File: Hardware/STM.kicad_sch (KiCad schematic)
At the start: 22 parts, among them SW1 Reset, U5 LM4040C33FTA, U6 STM32G484RETx

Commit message: Changes in CAN section
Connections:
- net STBY_CAN_1: now reaches U6.3 (PC14)
- net STBY_CAN_2: now reaches U6.4 (PC15)
- no-connect marks 23 -> 21
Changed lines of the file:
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@@
-	)
-	(no_connect
-		(at 121.92 119.38)
 	)
 	(no_connect
@@
 	(no_connect
 		(at 121.92 83.82)
-	)
-	(no_connect
-		(at 121.92 116.84)
 	)
 	(no_connect
@@
 	(wire
 		(pts
+			(xy 118.11 116.84) (xy 121.92 116.84)
+		)
+		(stroke
+			(width 0)
+			(type default)
+		)
+	)
+	(wire
+		(pts
 			(xy 186.69 27.94) (xy 186.69 30.48)
 		)
@@
 		(pts
 			(xy 186.69 35.56) (xy 186.69 39.37)
+		)
+		(stroke
+			(width 0)
+			(type default)
+		)
+	)
+	(wire
+		(pts
+			(xy 118.11 119.38) (xy 121.92 119.38)
 		)
 		(stroke
@@
 		(effects
 			(font
+				(size 1.27 1.27)
+			)
+			(justify right)
+		)
+	)
+	(hierarchical_label "STBY_CAN_2"
+		(shape output)
+		(at 118.11 119.38 180)
+		(effects
+			(font
+				(size 1.27 1.27)
+			)
+			(justify right)
+		)
+	)
+	(hierarchical_label "STBY_CAN_1"
+		(shape output)
+		(at 118.11 116.84 180)
+		(effects
+			(font

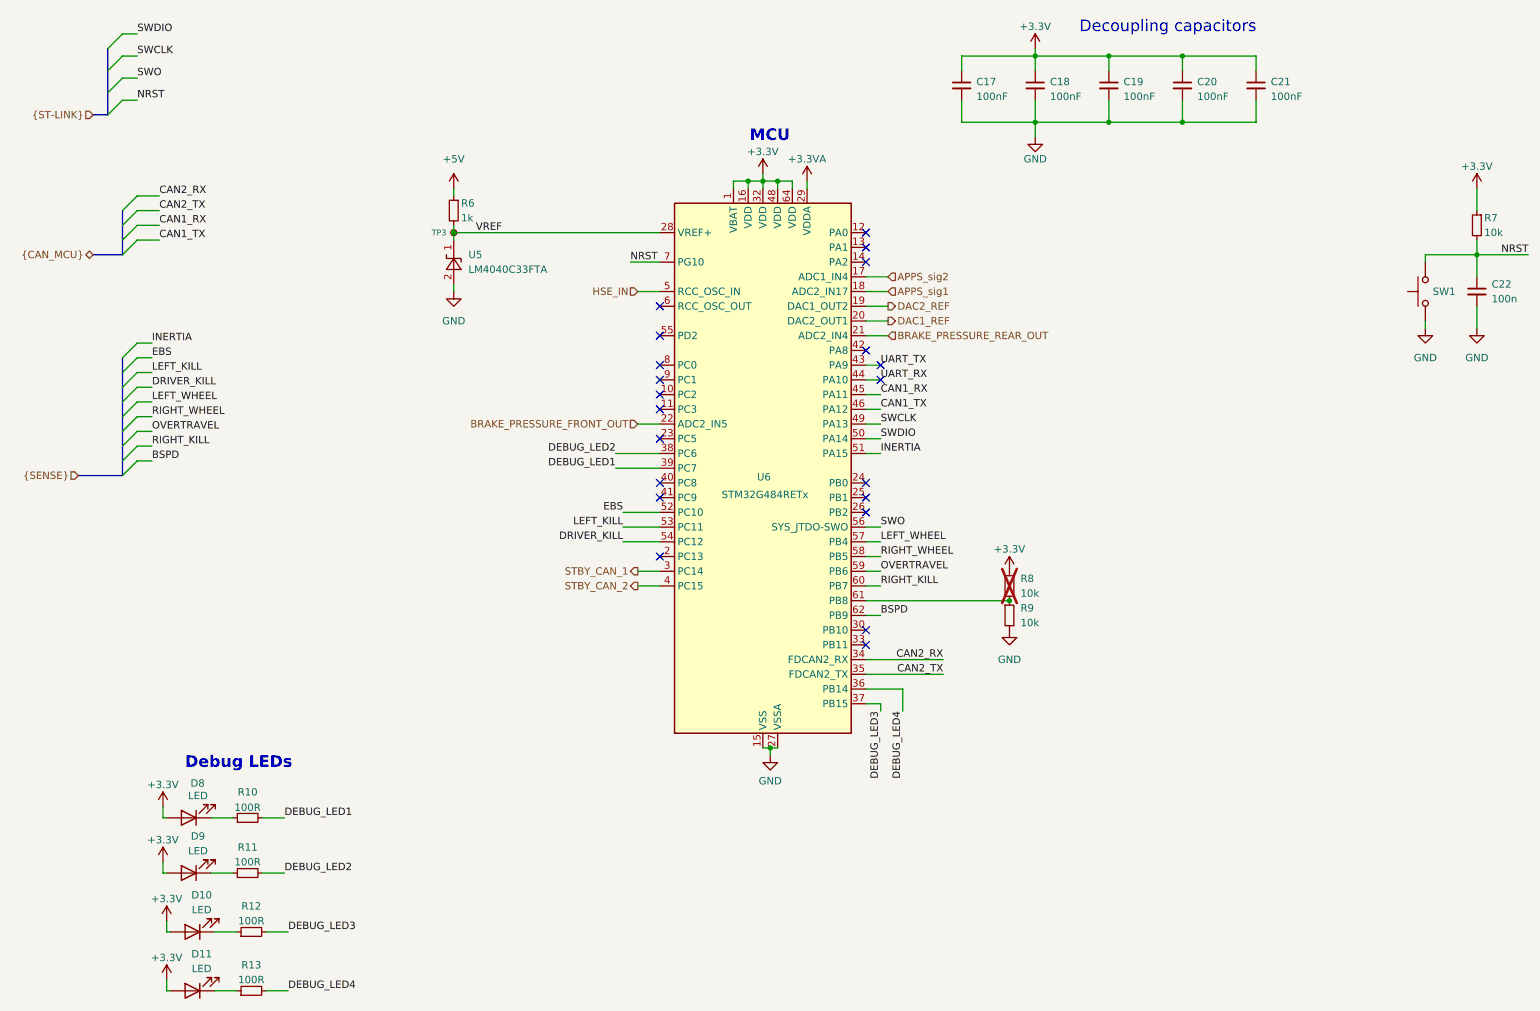
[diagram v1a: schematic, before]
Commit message: Changes in schematic, separated CAN buses, added XIAO Sense S3 DevBoard
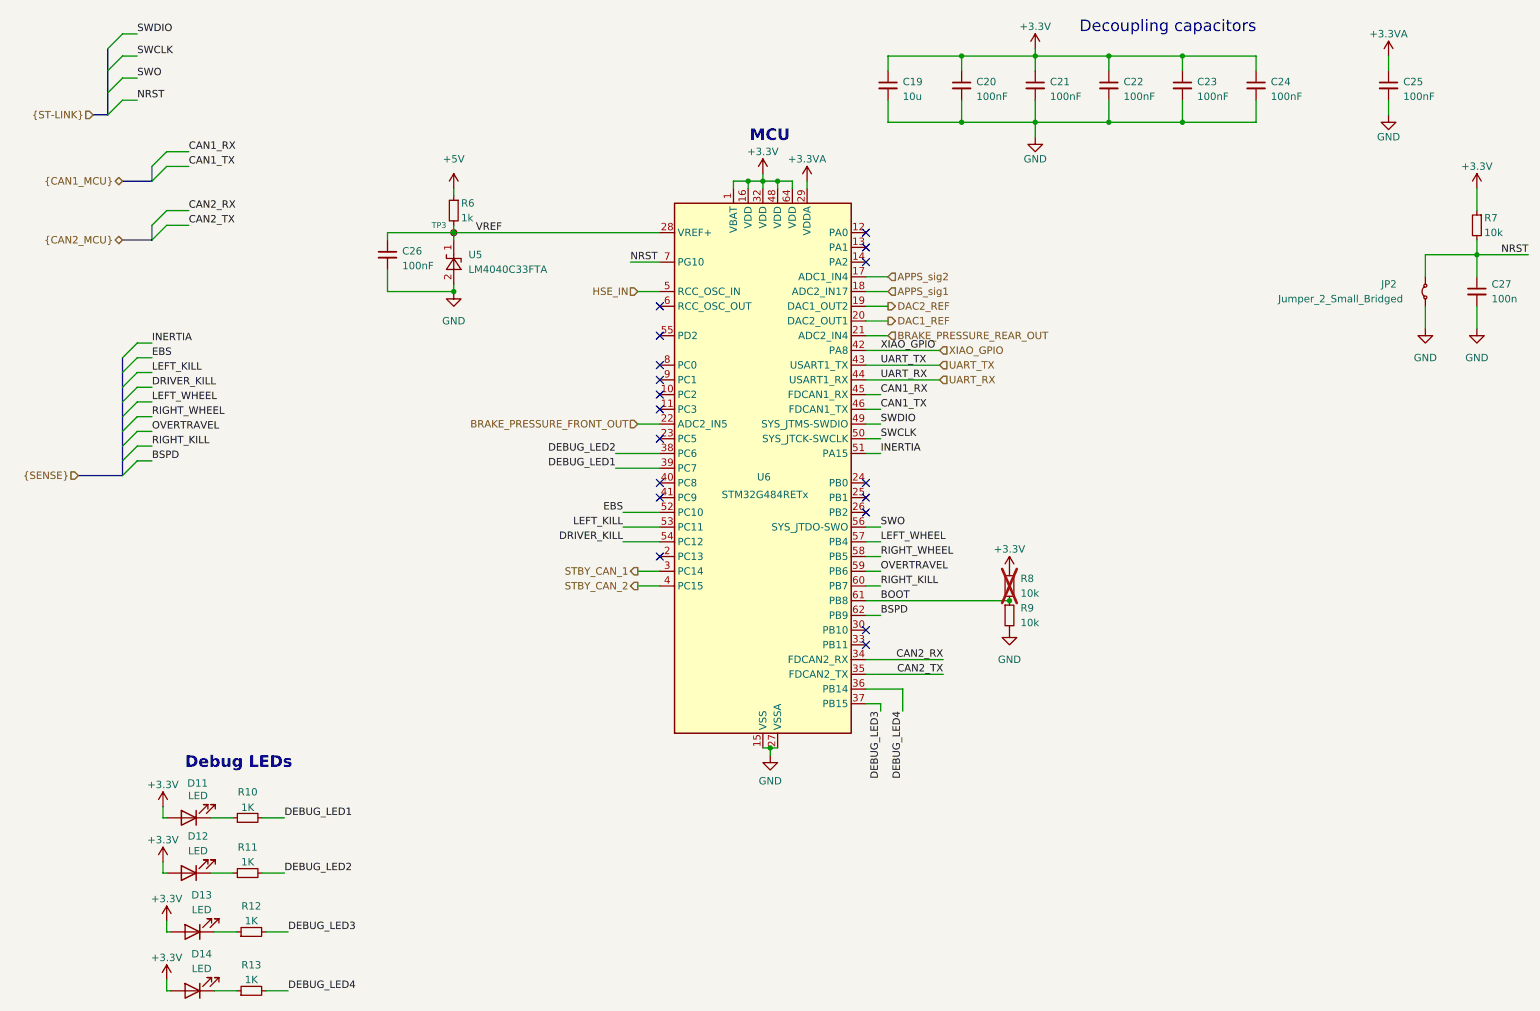
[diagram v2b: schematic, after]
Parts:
- removed SW1: Reset, Button_Switch_SMD:SW_SPST_B3U-1000P, symbol Switch:SW_Push
- added C19: 10u, Capacitor_SMD:C_0805_2012Metric_Pad1.18x1.45mm_HandSolder, symbol Device:C_Small
- added C25, C26: 100nF, Capacitor_SMD:C_0603_1608Metric_Pad1.08x0.95mm_HandSolder, symbol Device:C_Small
- added JP2: Jumper_2_Small_Bridged, Jumper:SolderJumper-2_P1.3mm_Open_TrianglePad1.0x1.5mm, symbol Jumper:Jumper_2_Small_Bridged
- R10, R11, R12, R13: value 100R -> 1K
- renumbered C17 to C20, C18 to C21, C19 to C22, C20 to C23, C21 to C24, C22 to C27, D8 to D11, D9 to D12, D10 to D13, D11 to D14
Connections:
- net +3.3V: now also C19.1
- net +3.3VA: now also C25.1
- net GND: now also C19.2, C25.2, C26.2, JP2.1 (A)
- net NRST: now also JP2.2 (B)
- net SWCLK: now also U6.50 (PA14); no longer U6.49 (PA13)
- net SWDIO: now also U6.49 (PA13); no longer U6.50 (PA14)
- net VREF: now also C26.1
- net BOOT: now reaches R8.2, R9.1, U6.61 (PB8)
- net XIAO_GPIO: now reaches U6.42 (PA8)
- no-connect marks 21 -> 18

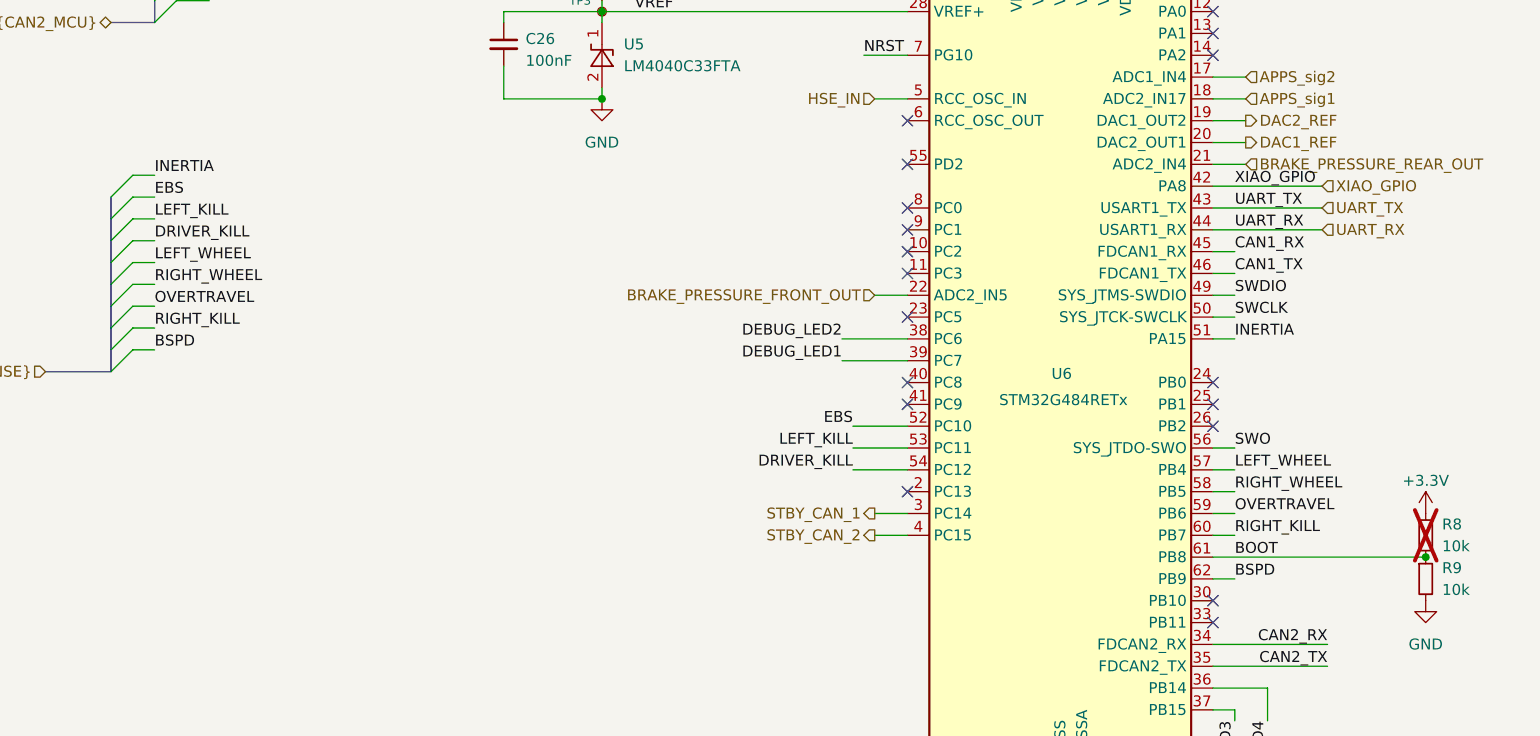
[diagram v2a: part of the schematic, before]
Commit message: Initial layout, changes in safety sensing bus labels
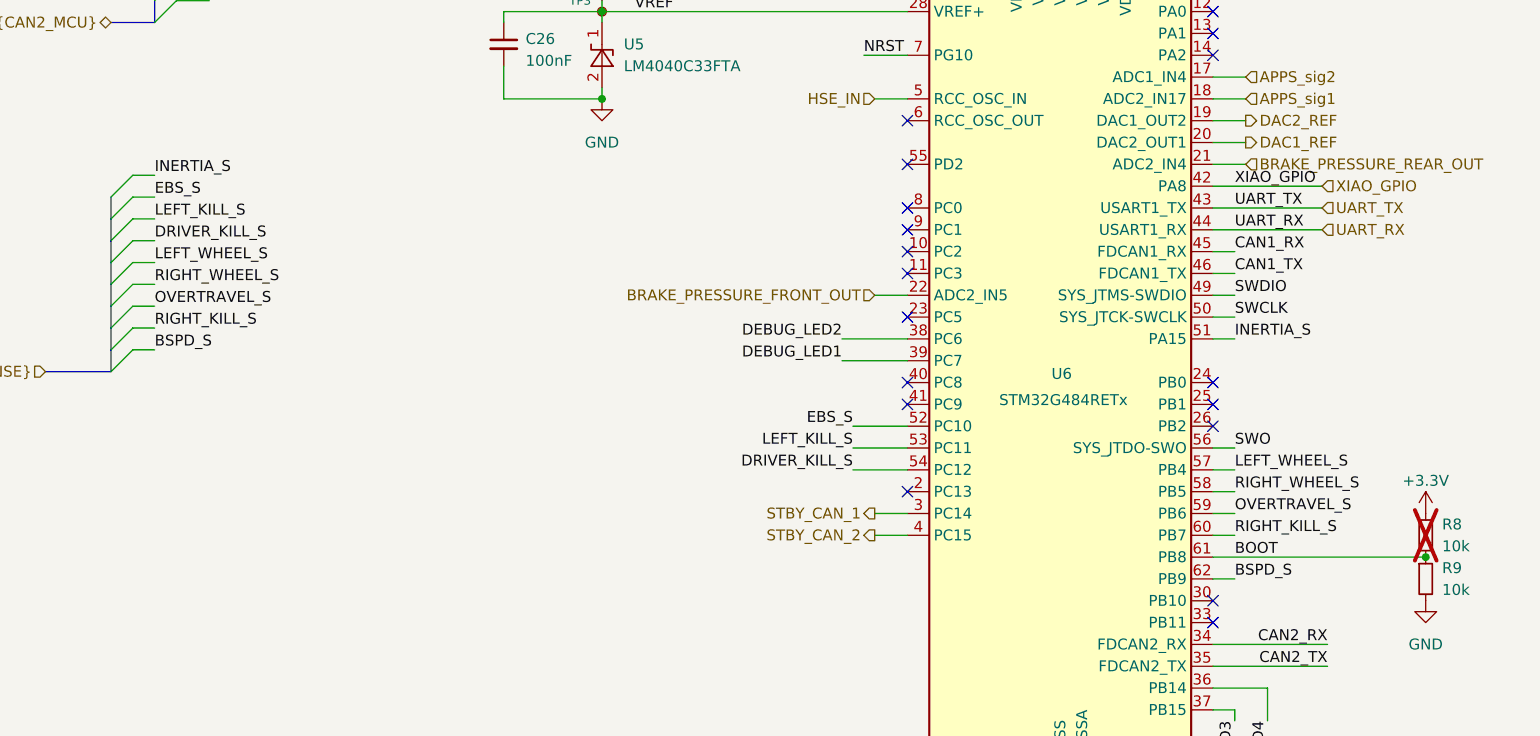
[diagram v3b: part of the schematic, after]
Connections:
- net BSPD renamed BSPD_S
- net DRIVER_KILL renamed DRIVER_KILL_S
- net EBS renamed EBS_S
- net INERTIA renamed INERTIA_S
- net LEFT_KILL renamed LEFT_KILL_S
- net LEFT_WHEEL renamed LEFT_WHEEL_S
- net OVERTRAVEL renamed OVERTRAVEL_S
- net RIGHT_KILL renamed RIGHT_KILL_S
- net RIGHT_WHEEL renamed RIGHT_WHEEL_S
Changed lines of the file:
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@@
 		)
 	)
-	(label "OVERTRAVEL"
+	(label "OVERTRAVEL_S"
 		(at 160.02 116.84 0)
 		(effects
@@
 		)
 	)
-	(label "LEFT_KILL"
+	(label "LEFT_KILL_S"
 		(at 115.57 109.22 180)
 		(effects
@@
 		)
 	)
-	(label "INERTIA"
+	(label "INERTIA_S"
 		(at 34.29 77.47 0)
 		(effects
@@
 		)
 	)
-	(label "BSPD"
+	(label "BSPD_S"
 		(at 34.29 97.79 0)
 		(effects
@@
 		)
 	)
-	(label "DRIVER_KILL"
+	(label "DRIVER_KILL_S"
 		(at 34.29 85.09 0)
 		(effects
@@
 		)
 	)
-	(label "EBS"
+	(label "EBS_S"
 		(at 34.29 80.01 0)
 		(effects
@@
 		)
 	)
-	(label "RIGHT_KILL"
+	(label "RIGHT_KILL_S"
 		(at 160.02 119.38 0)
 		(effects
@@
 		)
 	)
-	(label "EBS"
+	(label "EBS_S"
 		(at 115.57 106.68 180)
 		(effects
@@
 		)
 	)
-	(label "DRIVER_KILL"
+	(label "DRIVER_KILL_S"
 		(at 115.57 111.76 180)
 		(effects
@@
 		)
 	)
-	(label "LEFT_WHEEL"
+	(label "LEFT_WHEEL_S"
 		(at 160.02 111.76 0)
 		(effects
@@
 		)
 	)
-	(label "RIGHT_WHEEL"
+	(label "RIGHT_WHEEL_S"
 		(at 34.29 90.17 0)
 		(effects
@@
 		)
 	)
-	(label "INERTIA"
+	(label "INERTIA_S"
 		(at 160.02 96.52 0)
 		(effects
@@
 		)
 	)
-	(label "RIGHT_WHEEL"
+	(label "RIGHT_WHEEL_S"
 		(at 160.02 114.3 0)
 		(effects
@@
 		)
 	)
-	(label "BSPD"
+	(label "BSPD_S"
 		(at 160.02 124.46 0)
 		(effects
@@
 		)
 	)
-	(label "LEFT_WHEEL"
+	(label "LEFT_WHEEL_S"
 		(at 34.29 87.63 0)
 		(effects
@@
 		)
 	)
-	(label "RIGHT_KILL"
+	(label "RIGHT_KILL_S"
 		(at 34.29 95.25 0)
 		(effects
@@
 		)
 	)
-	(label "LEFT_KILL"
+	(label "LEFT_KILL_S"
 		(at 34.29 82.55 0)
 		(effects
@@
 		)
 	)
-	(label "OVERTRAVEL"
+	(label "OVERTRAVEL_S"
 		(at 34.29 92.71 0)
 		(effects

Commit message: Initial routing (Piotruś proszę nie bij że brzydko)
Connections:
- net UART_RX_PROG: now reaches U6.30 (PB10)
- net UART_TX_PROG: now reaches U6.9 (PC1)
- no-connect marks 18 -> 16
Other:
- moved on the sheet: R8, R9
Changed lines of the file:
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@@
 	)
 	(junction
-		(at 182.245 121.92)
+		(at 193.04 121.92)
 		(diameter 0)
 		(color 0 0 0 0)
@@
 	)
 	(no_connect
-		(at 157.48 127)
-	)
-	(no_connect
 		(at 157.48 60.96)
 	)
@@
 	)
 	(no_connect
-		(at 121.92 83.82)
-	)
-	(no_connect
 		(at 157.48 104.14)
 	)
@@
 	(wire
 		(pts
+			(xy 157.48 121.92) (xy 193.04 121.92)
+		)
+		(stroke
+			(width 0)
+			(type default)
+		)
+	)
+	(wire
+		(pts
 			(xy 147.32 49.53) (xy 147.32 50.8)
 		)
@@
 	(wire
 		(pts
-			(xy 157.48 121.92) (xy 182.245 121.92)
-		)
-		(stroke
-			(width 0)
-			(type default)
-		)
-	)
-	(wire
-		(pts
 			(xy 86.36 58.42) (xy 121.92 58.42)
 		)
@@
 	(wire
 		(pts
+			(xy 104.14 83.82) (xy 121.92 83.82)
+		)
+		(stroke
+			(width 0)
+			(type default)
+		)
+	)
+	(wire
+		(pts
 			(xy 186.69 27.94) (xy 186.69 30.48)
 		)
@@
 	(wire
 		(pts
+			(xy 193.04 129.54) (xy 193.04 127)
+		)
+		(stroke
+			(width 0)
+			(type default)
+		)
+	)
+	(wire
+		(pts
 			(xy 144.78 49.53) (xy 144.78 50.8)
 		)
@@
 	(wire
 		(pts
+			(xy 157.48 127) (xy 173.99 127)
+		)
+		(stroke
+			(width 0)
+			(type default)
+		)
+	)
+	(wire
+		(pts
 			(xy 140.97 147.32) (xy 142.24 147.32)
 		)
@@
 	)
 	(label "BOOT"
-		(at 160.02 121.92 0)
+		(at 175.895 121.92 0)
 		(effects
 			(font
@@
 		)
 	)
+	(label "UART_TX_PROG"
+		(at 118.11 83.82 180)
+		(effects
+			(font
+				(size 1.27 1.27)
+			)
+			(justify right bottom)
+		)
+	)
+	(label "UART_RX_PROG"
+		(at 160.02 127 0)
+		(effects
+			(font
+				(size 1.27 1.27)
+			)
+			(justify left bottom)
+		)
+	)
 	(label "RIGHT_WHEEL_S"
 		(at 160.02 114.3 0)
@@
 		)
 	)
+	(hierarchical_label "UART_RX_PROG"
+		(shape input)
+		(at 173.99 127 0)
+		(effects
+			(font
+				(size 1.27 1.27)
+			)
+			(justify left)
+		)
+	)
 	(hierarchical_label "UART_RX"
 		(shape input)
@@
 		)
 	)
+	(hierarchical_label "UART_TX_PROG"
+		(shape input)
+		(at 104.14 83.82 180)
+		(effects
+			(font
+				(size 1.27 1.27)
+			)
+			(justify right)
+		)
+	)
 	(hierarchical_label "HSE_IN"
 		(shape input)
@@
 	(symbol
 		(lib_id "power:GND")
-		(at 182.245 127 0)
+		(at 193.04 129.54 0)
 		(unit 1)
 		(exclude_from_sim no)
@@
 		(fields_autoplaced yes)
 		(property "Reference" "#PWR052"
-			(at 182.245 133.35 0)
+			(at 193.04 135.89 0)
 			(effects
 				(font
@@
 		)
 		(property "Value" "GND"
-			(at 182.245 132.08 0)
+			(at 193.04 134.62 0)
 			(effects
 				(font
@@
 		)
 		(property "Footprint" ""
-			(at 182.245 127 0)
+			(at 193.04 129.54 0)
 			(effects
 				(font
@@
 		)
 		(property "Datasheet" ""
-			(at 182.245 127 0)
+			(at 193.04 129.54 0)
 			(effects
 				(font
@@
 		)
 		(property "Description" ""
-			(at 182.245 127 0)
+			(at 193.04 129.54 0)
 			(effects
 				(font
@@
 	(symbol
 		(lib_id "Device:R_Small")
-		(at 182.245 124.46 0)
+		(at 193.04 124.46 0)
 		(unit 1)
 		(exclude_from_sim no)
@@
 		(fields_autoplaced yes)
 		(property "Reference" "R9"
-			(at 184.15 123.19 0)
+			(at 194.945 123.19 0)
 			(effects
 				(font
@@
 		)
 		(property "Value" "10k"
-			(at 184.15 125.73 0)
+			(at 194.945 125.73 0)
 			(effects
 				(font
@@
 		)
 		(property "Footprint" "Resistor_SMD:R_0603_1608Metric"
-			(at 182.245 124.46 0)
+			(at 193.04 124.46 0)
 			(effects
 				(font
@@
 		)
 		(property "Datasheet" "~"
-			(at 182.245 124.46 0)
+			(at 193.04 124.46 0)
 			(effects
 				(font
@@
 		)
 		(property "Description" ""
-			(at 182.245 124.46 0)
+			(at 193.04 124.46 0)
 			(effects
 				(font
@@
 	(symbol
 		(lib_id "Device:R_Small")
-		(at 182.245 119.38 0)
+		(at 193.04 119.38 0)
 		(unit 1)
 		(exclude_from_sim no)
@@
 		(fields_autoplaced yes)
 		(property "Reference" "R8"
-			(at 184.15 118.11 0)
+			(at 194.945 118.11 0)
 			(effects
 				(font
@@
 		)
 		(property "Value" "10k"
-			(at 184.15 120.65 0)
+			(at 194.945 120.65 0)
 			(effects
 				(font
@@
 		)
 		(property "Footprint" "Resistor_SMD:R_0603_1608Metric"
-			(at 182.245 119.38 0)
+			(at 193.04 119.38 0)
 			(effects
 				(font
@@
 		)
 		(property "Datasheet" "~"
-			(at 182.245 119.38 0)
+			(at 193.04 119.38 0)
 			(effects
 				(font
@@
 		)
 		(property "Description" ""
-			(at 182.245 119.38 0)
+			(at 193.04 119.38 0)
 			(effects
 				(font
@@
 		)
 		(pin "9"
+			(alternate "LPUART1_TX")
 		)
 		(pin "31"
@@
 		)
 		(pin "30"
+			(alternate "LPUART1_RX")
 		)
 		(pin "33"
@@
 	(symbol
 		(lib_id "power:+3.3V")
-		(at 182.245 116.84 0)
+		(at 193.04 116.84 0)
 		(unit 1)
 		(exclude_from_sim no)
@@
 		(fields_autoplaced yes)
 		(property "Reference" "#PWR051"
-			(at 182.245 120.65 0)
+			(at 193.04 120.65 0)
 			(effects
 				(font
@@
 		)
 		(property "Value" "+3.3V"
-			(at 182.245 113.03 0)
+			(at 193.04 113.03 0)
 			(effects
 				(font
@@
 		)
 		(property "Footprint" ""
-			(at 182.245 116.84 0)
+			(at 193.04 116.84 0)
 			(effects
 				(font
@@
 		)
 		(property "Datasheet" ""
-			(at 182.245 116.84 0)
+			(at 193.04 116.84 0)
 			(effects
 				(font
@@
 		)
 		(property "Description" ""
-			(at 182.245 116.84 0)
+			(at 193.04 116.84 0)
 			(effects
 				(font
